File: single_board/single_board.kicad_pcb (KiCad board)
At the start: 4 copper layers, 114 parts, among them J1 CAN_OUT, J10 SPI Debug, J11 Screw_Terminal_01x02, J12 Conn_01x03, J13 Conn_01x04, J14 Screw_Terminal_01x02, J15 UART, J16 BOOTSEL, J17 Conn_01x03, J18 Conn_01x04, J19 Conn_01x03, J2 USB_C_Receptacle_USB2.0_16P, J20 Screw_Terminal_01x02, J21 Conn_01x04, J22 Conn_01x03, J23 Conn_01x04, J24 Screw_Terminal_01x02, J25 Conn_01x03, J26 Conn_01x04, J27 Screw_Terminal_01x02, J28 Screw_Terminal_01x02, J3 Conn_01x02, J5 490107670612, J6 Screw_Terminal_01x02, J7 Conn_01x03, J8 Conn_01x04, J9 SWD, Q1 AO3401A, Q2 2N7002, Q3 AO3401A, Q4 AO3401A, Q5 AO3401A, SW1 Button, U1 AP2112K-3.3, U2 TJA1042T-3, U3 USBLC6-2SC6, U4 LSM6DSV, U5 STM32G474VBTx, Y1 FC-135

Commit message: IMU
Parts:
- added D5: LED, LED_SMD:LED_0603_1608Metric_Pad1.05x0.95mm_HandSolder, F.Cu at (95.5, 169.0)
- added D6: LED, LED_SMD:LED_0603_1608Metric_Pad1.05x0.95mm_HandSolder, F.Cu at (95.5, 171.6)
- added R29: 10k, Resistor_SMD:R_0402_1005Metric_Pad0.72x0.64mm_HandSolder, F.Cu at (99.3, 168.7)
- added R30: 10k, Resistor_SMD:R_0402_1005Metric_Pad0.72x0.64mm_HandSolder, F.Cu at (99.3, 170.7)
- moved R7 91.1 mm to (98.5, 161.9)
- moved D1 91.1 mm to (95.3, 161.8)
- moved D7 42.4 mm to (96.1, 165.7), turned to 180 degrees
- moved R20 37.8 mm to (99.4, 165.7), turned to 0 degrees
- moved R21 22.3 mm to (108.6, 90.8), turned to 90 degrees
- moved J16 19.5 mm to (108.6, 94.6), turned to 90 degrees
- moved R19 16.7 mm to (113.7, 90.9), turned to -90 degrees
- moved C13 7.65 mm to (146.7, 100.3)
- moved C12 7.65 mm to (149.1, 100.3)
- moved J11 7.41 mm to (138.2, 153.4)
- moved J20 7.41 mm to (156.3, 153.5)
- moved J24 7.41 mm to (165.9, 153.5)
- moved J6 7.41 mm to (129.8, 153.4)
- moved Q2 7.41 mm to (165.7, 147.2)
- moved R16 7.41 mm to (140.9, 141.7)
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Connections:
- J20 pad 1: /FSR -> /FSR_ADC
- R23 pad 1: /FSR -> /FSR_ADC
- U5 pad 44: /FSR_SIG -> /FSR_ADC
- U5 pad 45: /FSR -> /FSR_SIG
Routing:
- net /IMU_NSS: track 4.69 -> 18.3 mm
- net /IMU_SCK: track 4.69 -> 17.8 mm
- net /IMU_MOSI: track 4.77 -> 17.3 mm, vias 0 -> 2
- net /IMU_MISO: track 4.94 -> 16.1 mm, vias 0 -> 2
- net /BOOT0: track 5.48 -> 14.2 mm
- net /TRI_LED_R: track 6.60 -> 13.5 mm
- net /FSR: track 6.92 -> 0.00 mm
- net /FSR_ADC: track 0.00 -> 6.59 mm
- net /TRI_LED_B: track 6.10 -> 12.7 mm
- net /INT1: track 4.69 -> 11.0 mm, vias 0 -> 2
- net /INT2: track 4.94 -> 11.0 mm, vias 0 -> 2
- net /TRI_LED_G: track 5.60 -> 11.6 mm
- net /PWM6: track 5.43 -> 8.83 mm
- net /DIR6: track 6.65 -> 8.58 mm
- net v3v3: vias 16 -> 17
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
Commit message: End effector gpio
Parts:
- moved D5 30.4 mm to (119.1, 149.8)
- moved D6 30.4 mm to (119.1, 152.4)
- moved R7 30.4 mm to (122.1, 142.8)
- moved D1 30.4 mm to (118.9, 142.7)
- moved R29 30.4 mm to (122.9, 149.5)
- moved R30 30.4 mm to (122.9, 151.5)
- moved D7 30.4 mm to (119.6, 146.6)
- moved R20 30.4 mm to (123.0, 146.6)
- moved J16 22.6 mm to (131.1, 93.3), turned to 180 degrees
- moved R21 18.9 mm to (127.3, 93.3), turned to 180 degrees
- moved R24 16.2 mm to (155.2, 128.5), turned to 90 degrees
- moved R14 14.4 mm to (144.1, 131.6)
- moved J24 14.0 mm to (159.5, 141.0)
- moved R19 13.9 mm to (127.4, 88.2), turned to 0 degrees
- moved Q2 13.6 mm to (159.5, 135.1)
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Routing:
- net /FSR_ADC: track 6.59 -> 10.6 mm
- net /LASER_SIG: track 6.57 -> 9.77 mm
- net /FSR_SIG: track 6.92 -> 10.1 mm
- net /LS1: track 6.44 -> 7.41 mm
- net /LS2: track 6.96 -> 7.49 mm
- net v3v3: vias 17 -> 21
- net GND: vias 29 -> 33
- added copper zone on F.Cu, net v3v3

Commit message: Layout pass 3
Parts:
- removed the R12 at (134.1, 136.3)
- removed the R14 at (144.1, 131.6)
- removed the R15 at (140.8, 136.3)
- removed the R16 at (146.3, 131.6)
- removed the R17 at (147.5, 136.3)
- removed the R2 at (141.2, 93.7)
- removed the R5 at (137.8, 93.7)
- removed the R8 at (139.6, 93.7)
- added R20: 120, Resistor_SMD:R_0402_1005Metric_Pad0.72x0.64mm_HandSolder, F.Cu at (139.1, 132.1)
- added R21: 1k, Capacitor_SMD:C_0402_1005Metric_Pad0.74x0.62mm_HandSolder, F.Cu at (140.5, 136.3)
- added R22: 120, Resistor_SMD:R_0402_1005Metric_Pad0.72x0.64mm_HandSolder, F.Cu at (143.4, 132.1)
- added R24: 1k, Capacitor_SMD:C_0402_1005Metric_Pad0.74x0.62mm_HandSolder, F.Cu at (147.0, 136.4)
- added R25: 120, Resistor_SMD:R_0402_1005Metric_Pad0.72x0.64mm_HandSolder, F.Cu at (147.8, 132.1)
- added R3: 1k, Capacitor_SMD:C_0402_1005Metric_Pad0.74x0.62mm_HandSolder, F.Cu at (138.0, 94.4)
- added R7: 1k, Capacitor_SMD:C_0402_1005Metric_Pad0.74x0.62mm_HandSolder, F.Cu at (139.3, 94.4)
- added R9: 1k, Capacitor_SMD:C_0402_1005Metric_Pad0.74x0.62mm_HandSolder, F.Cu at (136.7, 94.4)
- R18: value 120 -> 1k; footprint Resistor_SMD:R_0402_1005Metric_Pad0.72x0.64mm_HandSolder -> Capacitor_SMD:C_0402_1005Metric_Pad0.74x0.62mm_HandSolder
- moved H1 157.3 mm to (113.8, 83.5)
- moved H2 149.6 mm to (113.7, 145.8)
- moved H3 89.0 mm to (199.7, 83.6)
- moved H4 63.5 mm to (200.1, 145.1)
- moved D2 62.5 mm to (181.8, 140.2), turned to 90 degrees
- moved R2 58.9 mm to (181.8, 143.5), turned to -90 degrees
- moved D1 48.2 mm to (167.0, 140.1), turned to 90 degrees
- moved R1 44.9 mm to (166.9, 143.3), turned to -90 degrees
- moved J20 43.6 mm to (195.5, 120.0)
- moved C34 39.4 mm to (194.9, 137.8)
- moved C35 39.4 mm to (194.9, 126.5)
- moved J22 39.4 mm to (195.7, 135.1)
- moved J24 39.4 mm to (195.5, 124.0)
- moved C7 38.5 mm to (178.6, 105.5), turned to 90 degrees
- moved J23 38.0 mm to (195.8, 131.2)
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- renumbered D7 to D2, D2 to D3, D5 to D4, D6 to D5, D3 to D6, D4 to D7, J9 to J10, J10 to J11, J11 to J12, J12 to J13, J13 to J14, J14 to J15, J15 to J16, J16 to J17, J17 to J18, J18 to J19, J19 to J20, J20 to J21, J21 to J22, J22 to J23, J23 to J24, J24 to J25, J25 to J26, J26 to J27, J27 to J3, J3 to J4, J28 to J5, J5 to J6, J6 to J7, J7 to J8, J8 to J9, Q3 to Q1, Q4 to Q2, Q5 to Q3, Q1 to Q4, Q2 to Q5, R7 to R1, R9 to R10, R29 to R11, R30 to R12, R28 to R13, R10 to R14, R11 to R15, R25 to R16, R26 to R17, R13 to R19, R20 to R2, R27 to R23, R19 to R26, R21 to R27, R22 to R28, R23 to R29, R24 to R30, R1 to R4, R3 to R5, R4 to R6, R6 to R8
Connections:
- D3 pad 3: 5V -> v3v3
- D4 pad 2: unconnected-(D5-A-Pad2) -> /LED1
- D5 pad 2: unconnected-(D6-A-Pad2) -> /LED2
- R18 pad 1: /LimitSwitch3 -> v3v3
- R18 pad 2: /LS3 -> /LimitSwitch1
- U5 pad 30: /HEARTBEAT -> /LED1
- U5 pad 31: unconnected-(U5-PC5-Pad31) -> /LED2
- U5 pad 58: unconnected-(U5-PD11-Pad58) -> /HEARTBEAT
- U5 pad 92: /TRI_LED_R -> /TRI_LED_G
- U5 pad 93: /TRI_LED_B -> /TRI_LED_R
- U5 pad 94: /TRI_LED_G -> /TRI_LED_B
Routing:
- net /CAN_STB: track 6.27 -> 17.3 mm
- net /FDCAN_TX: track 6.34 -> 11.3 mm
- net /LED1: track 0.00 -> 4.71 mm
- net /HEARTBEAT: track 4.71 -> 0.00 mm
- net /FDCAN_RX: track 5.94 -> 9.92 mm
- net /TRI_LED_G: track 11.6 -> 13.5 mm
- net /TRI_LED_B: track 12.7 -> 11.6 mm
- net /TRI_LED_R: track 13.5 -> 12.7 mm
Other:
- board outline added: 94.5 x 70.3 mm

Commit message: Pos
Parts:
- moved R19 34.7 mm to (142.7, 88.2), turned to 180 degrees
- moved C28 33.1 mm to (142.7, 86.2), turned to 180 degrees
- moved SW1 28.2 mm to (147.8, 87.2), turned to 180 degrees
- moved D2 27.5 mm to (158.9, 124.9)
- moved R2 27.5 mm to (158.9, 128.2)
- moved D1 16.0 mm to (161.8, 125.0)
- moved R1 16.0 mm to (161.7, 128.2)
- moved Q3 11.4 mm to (168.7, 86.5), turned to 180 degrees
- moved H4 10.2 mm to (189.9, 144.8)
- moved J6 9.89 mm to (160.3, 87.4), turned to -90 degrees
- moved D6 9.65 mm to (173.8, 92.0)
- moved D7 9.65 mm to (173.8, 99.1)
- moved J3 9.65 mm to (188.2, 90.1)
- moved J4 9.65 mm to (182.0, 90.0)
- moved J5 9.65 mm to (188.2, 97.0)
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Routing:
- net /LED2: track 0.00 -> 5.63 mm
- net /LED1: track 4.71 -> 4.11 mm
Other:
- board size 94.5 x 70.3 mm -> 85.3 x 71.2 mm

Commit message: Signal Traces
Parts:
- moved D4 5.95 mm to (120.8, 140.6)
- moved R11 5.95 mm to (120.7, 143.6)
- moved D5 3.43 mm to (125.8, 140.6)
- moved R12 3.43 mm to (125.8, 143.7)
- moved C2 0.84 mm to (166.7, 128.3)
- moved C8 0.84 mm to (170.8, 139.2)
- moved C9 0.84 mm to (165.5, 131.5)
- moved R10 0.84 mm to (170.2, 137.4)
- moved R5 0.84 mm to (171.0, 136.4)
- moved R8 0.84 mm to (170.5, 134.6)
- moved U2 0.84 mm to (170.5, 129.8)
- moved C1 0.83 mm to (165.6, 128.3)
- moved C10 0.83 mm to (166.6, 131.5)
- moved R24 0.83 mm to (147.8, 136.3)
- moved R25 0.75 mm to (148.5, 132.1), turned to 90 degrees
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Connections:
- U5 pad 50: /CAN_LED -> unconnected-(U5-PB11-Pad50)
- U5 pad 54: unconnected-(U5-PB15-Pad54) -> /CAN_LED
- U5 pad 55: unconnected-(U5-PD8-Pad55) -> /HEARTBEAT
- U5 pad 58: /HEARTBEAT -> unconnected-(U5-PD11-Pad58)
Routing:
- net /RST: track 1.67 -> 74.2 mm, vias 1 -> 2
- net /PWM5: track 8.19 -> 39.4 mm
- net /PWM4: track 6.98 -> 37.0 mm
- net /ENC4_B: track 9.40 -> 37.9 mm
- net /ENC5_B: track 7.02 -> 34.7 mm
- net /LED1: track 4.11 -> 31.7 mm, vias 0 -> 2
- net /DIR5: track 8.92 -> 36.4 mm
- net /ENC4_A: track 9.01 -> 35.7 mm
- net /DIR4: track 7.06 -> 33.3 mm
- net 5V: track 0.00 -> 26.2 mm, vias 0 -> 2
- net /ENC5_A: track 7.08 -> 32.1 mm
- net /ENC3_B: track 4.57 -> 29.5 mm
- net /LED2: track 5.63 -> 27.7 mm, vias 0 -> 2
- net /PWM6: track 8.83 -> 30.4 mm
- net /SWDIO: track 6.43 -> 26.7 mm
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- added copper zone on B.Cu, net GND
- added copper zone on F.Cu, net GND
- added copper zone on In2.Cu, net GND
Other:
- board size 85.3 x 71.2 mm -> 90 x 70 mm

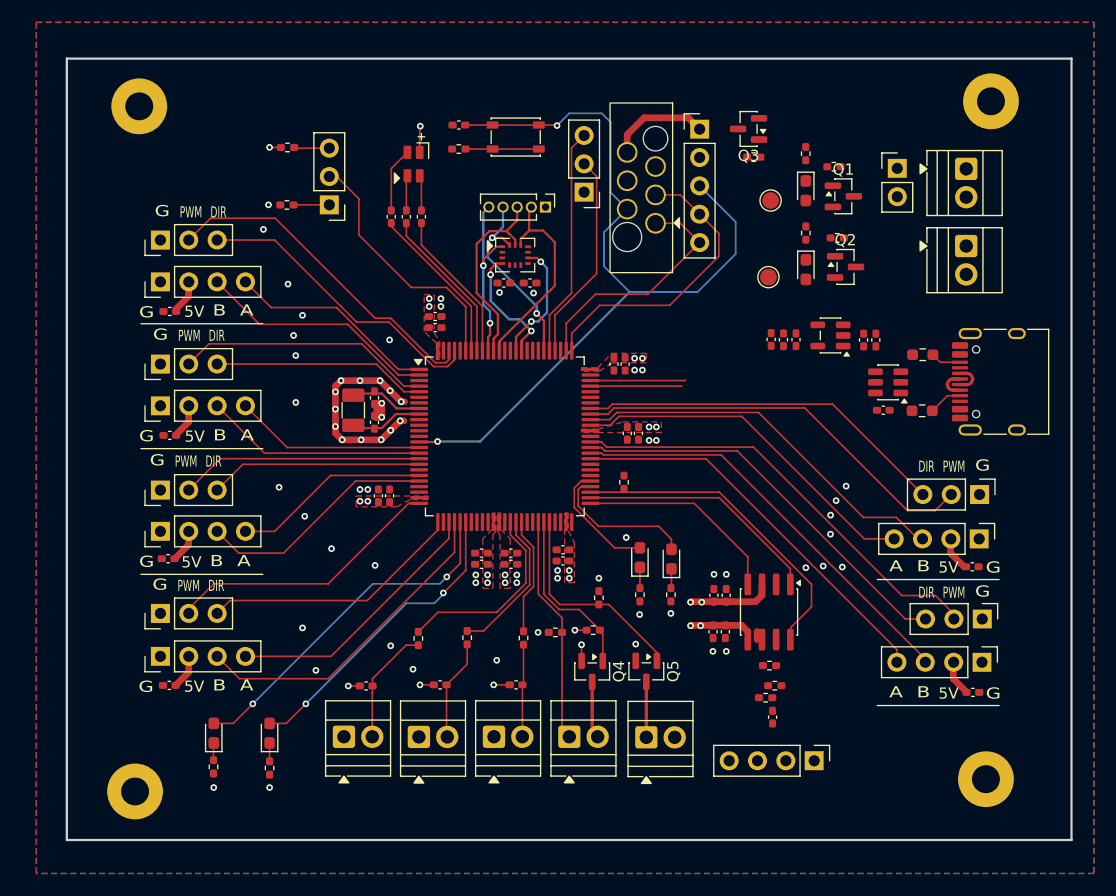
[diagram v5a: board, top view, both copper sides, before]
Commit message: Diff pairs, layer 1 power
Net classes and rules
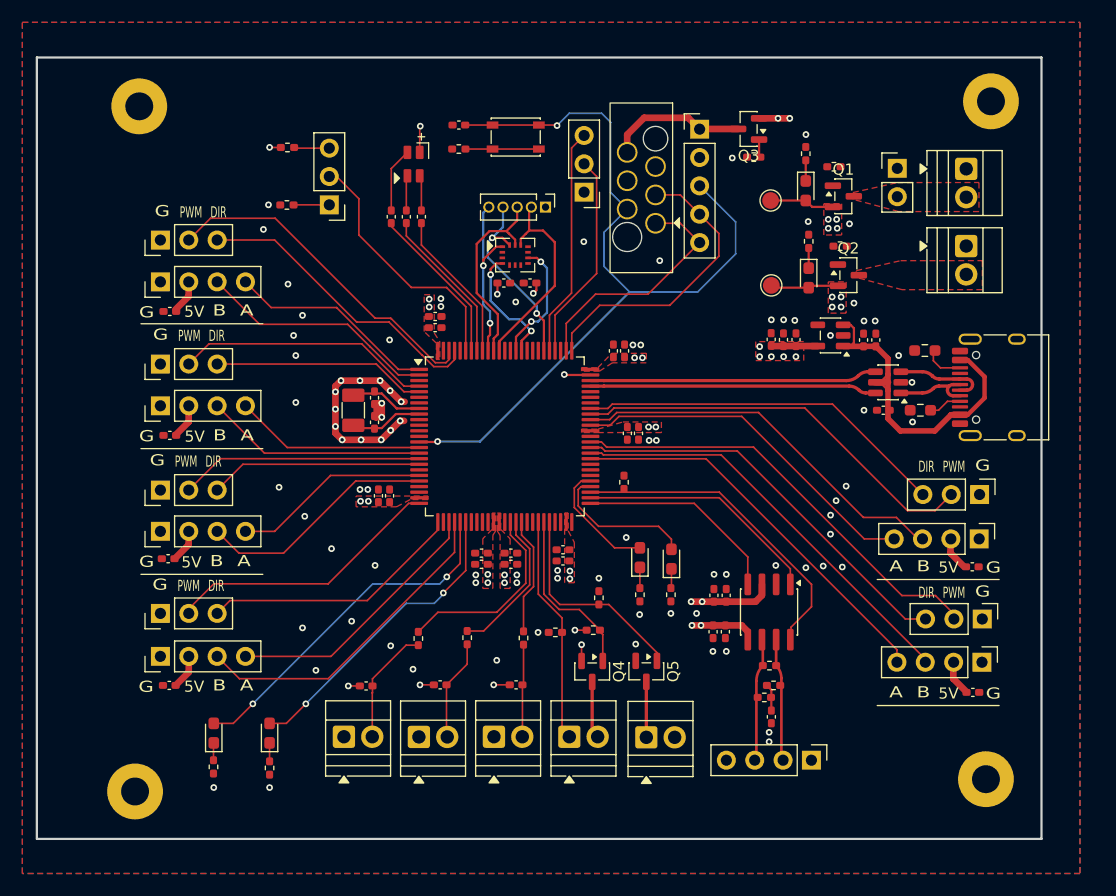
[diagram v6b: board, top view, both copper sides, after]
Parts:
- moved C15 1.19 mm to (157.6, 106.4), turned to 90 degrees
- moved C21 1.19 mm to (156.6, 106.4), turned to 90 degrees
- moved R17 0.78 mm to (176.9, 97.0)
- moved D7 0.78 mm to (174.0, 99.8)
- moved Q2 0.78 mm to (177.6, 99.6)
- moved R15 0.78 mm to (174.0, 96.6)
- moved TP2 0.78 mm to (170.7, 100.5)
- moved J2 0.50 mm to (191.6, 109.7)
- moved R6 0.42 mm to (184.4, 106.3)
- moved J1 0.25 mm to (174.3, 143.1)
- moved R4 0.17 mm to (184.1, 111.7)
- moved C8 0.11 mm to (170.7, 139.2)
- moved R10 0.11 mm to (170.1, 137.4)
- moved R5 0.11 mm to (170.9, 136.3)
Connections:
- net Net-(J2-D+-PadA6) renamed /DP
- net Net-(J2-D--PadA7) renamed /DN
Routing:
- net 5V: track 26.2 -> 63.8 mm, vias 2 -> 6
- net /USB-DN: track 8.21 -> 25.7 mm
- net /USB-DP: track 8.52 -> 25.7 mm
- net v3v3: track 15.0 -> 29.9 mm, vias 9 -> 37
- net /can_DP: track 0.00 -> 11.0 mm
- net /can_DN: track 0.72 -> 11.0 mm
- net /DP: track 2.93 -> 8.40 mm
- net /DN: track 2.93 -> 7.42 mm
- net /v3v3IN: track 9.13 -> 12.6 mm
- net Net-(C8-Pad1): track 0.00 -> 2.42 mm
- net GND: track 22.3 -> 24.7 mm, vias 81 -> 88
- net Net-(D6-K): track 0.00 -> 1.85 mm
- net Net-(D7-K): track 0.00 -> 1.80 mm
- net Net-(Q3-G): track 0.00 -> 1.62 mm
- net Net-(J2-CC2): track 2.70 -> 3.63 mm
- added copper zone on F.Cu, net /5VIN
- added copper zone on F.Cu, net 5V
- added copper zone on In1.Cu, net 5V
- added copper zone on In1.Cu, net v3v3

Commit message: 80x80
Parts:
- moved J4 59.6 mm to (217.5, 137.9)
- moved TP1 59.6 mm to (206.2, 140.8)
- moved D6 59.6 mm to (209.3, 139.9)
- moved J3 59.6 mm to (223.7, 138.0)
- moved Q1 59.6 mm to (212.7, 140.4)
- moved R14 59.6 mm to (209.3, 136.6)
- moved R16 59.6 mm to (211.8, 137.8)
- moved H2 9.48 mm to (120.4, 152.6)
- moved H4 7.81 mm to (190.4, 152.6)
- moved H1 6.61 mm to (120.4, 82.5)
- moved C4 5.51 mm to (173.4, 105.3)
- moved C3 5.51 mm to (174.6, 105.3)
- moved C5 5.51 mm to (167.4, 105.2)
- moved C6 5.51 mm to (166.3, 105.2)
- moved C7 5.51 mm to (165.2, 105.2)
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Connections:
- J10 pad 1: /v3v3IN -> /v3v3IN_debug
- J6 pad 6: /v3v3IN -> /v3v3IN_debug
- Q3 pad 3: /v3v3IN -> /v3v3IN_debug
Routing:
- net v3v3: track 29.9 -> 274.7 mm, vias 37 -> 36
- net 5V: track 63.8 -> 141.6 mm, vias 6 -> 10
- net /v3v3IN_debug: track 0.00 -> 12.6 mm
- net /v3v3IN: track 12.6 -> 0.00 mm
- net Net-(Q1-G): track 0.00 -> 1.91 mm
- net Net-(Q2-G): track 0.00 -> 1.82 mm
- net GND: vias 88 -> 98
- added copper zone on F.Cu, net /v3v3IN
- added copper zone on In2.Cu, net 5V
- added copper zone on In2.Cu, net v3v3
- removed copper zone on In1.Cu, net 5V
- removed copper zone on In1.Cu, net v3v3
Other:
- board size 90 x 70 mm -> 80 x 80 mm

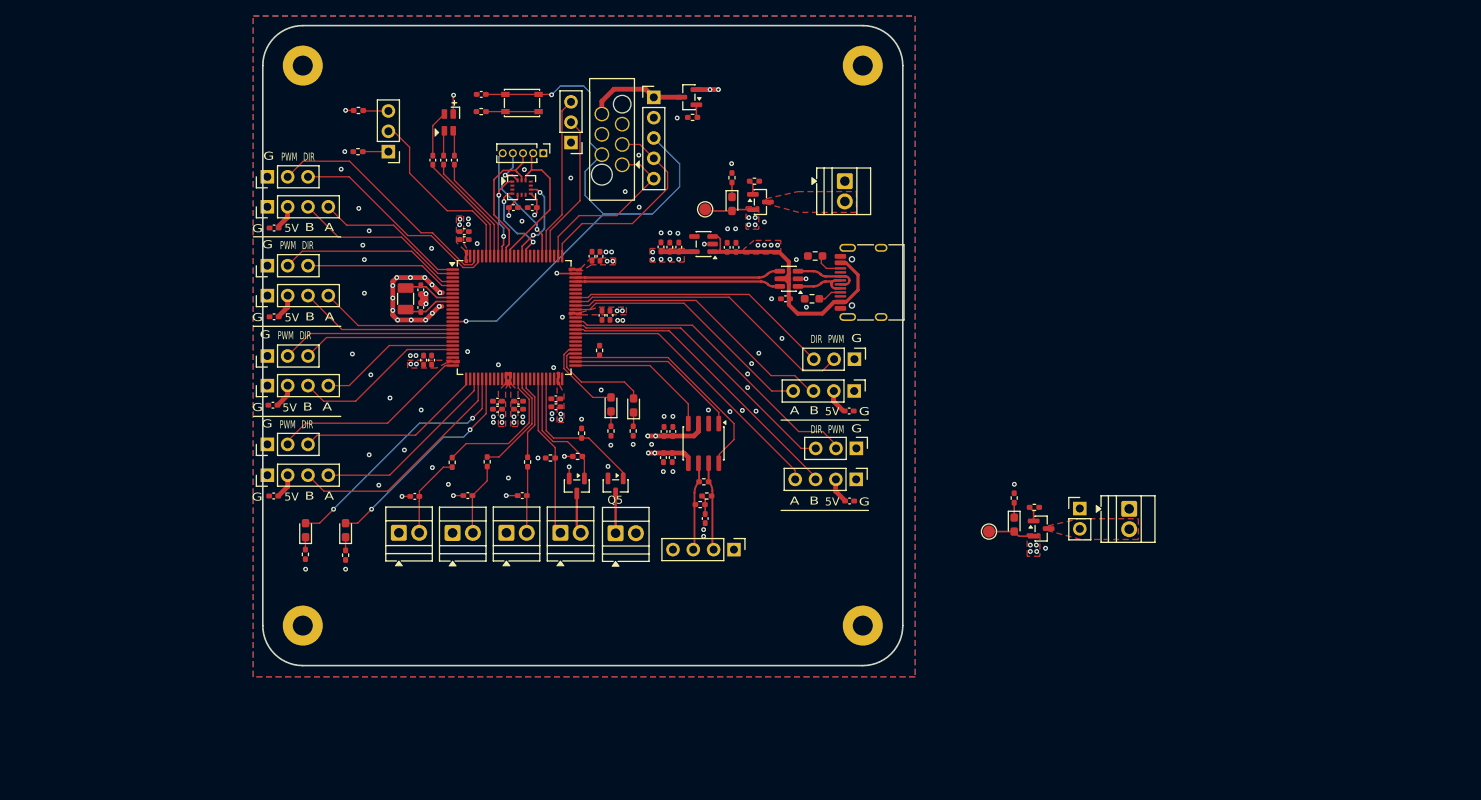
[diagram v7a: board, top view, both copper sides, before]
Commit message: All sig
todo: power, silkscreen, vias
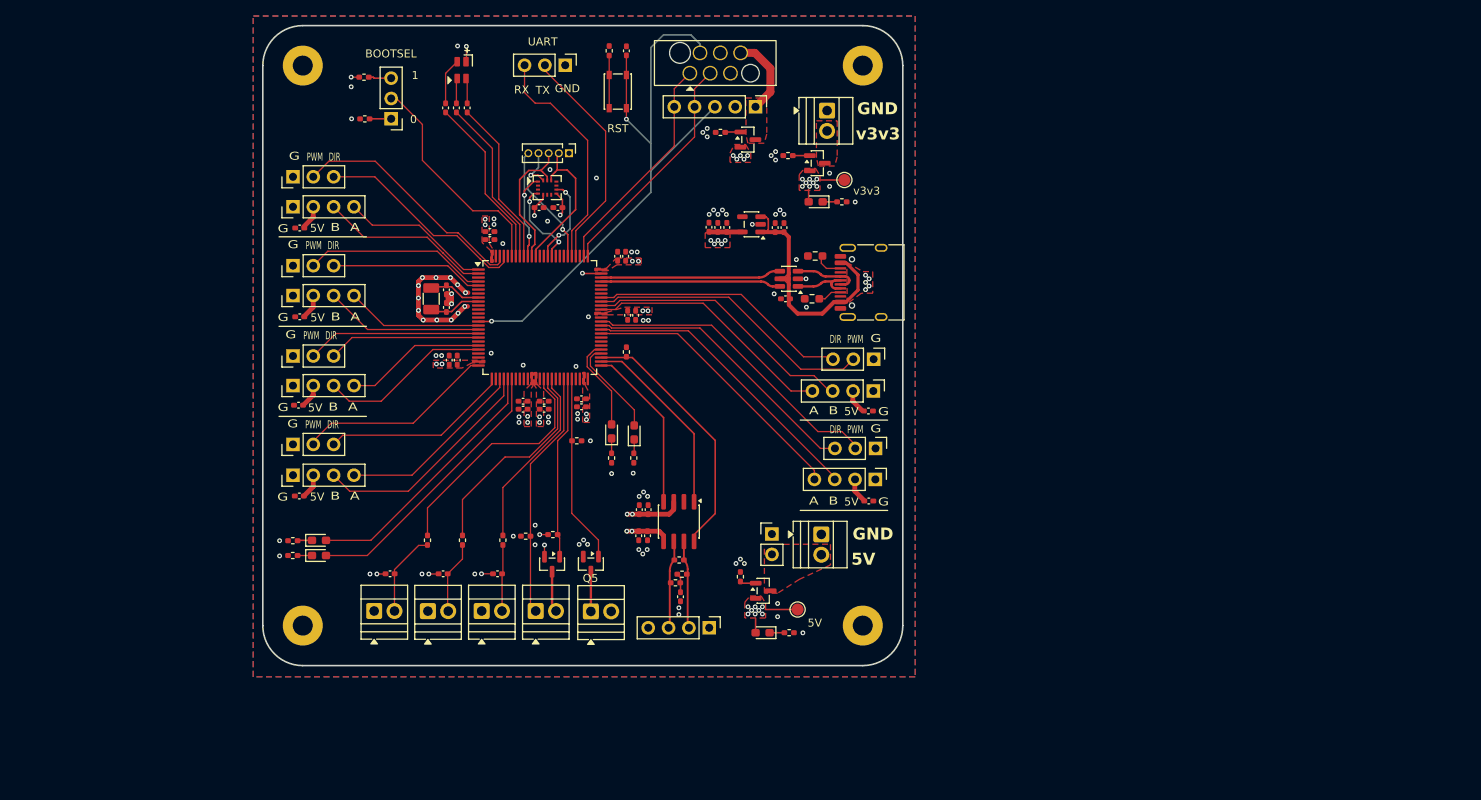
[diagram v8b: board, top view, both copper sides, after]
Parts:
- moved J4 38.6 mm to (179.0, 141.1)
- moved J3 38.6 mm to (185.2, 141.2)
- moved R16 37.8 mm to (175.1, 146.4), turned to 90 degrees
- moved Q1 35.6 mm to (177.9, 148.2)
- moved D6 34.2 mm to (177.9, 153.4), turned to 180 degrees
- moved R14 32.8 mm to (181.2, 153.4), turned to 0 degrees
- moved TP1 25.8 mm to (182.2, 150.5)
- moved C28 18.9 mm to (160.8, 80.7), turned to 90 degrees
- moved TP2 17.8 mm to (188.1, 96.8), turned to -90 degrees
- moved R19 17.7 mm to (158.7, 80.7), turned to 90 degrees
- moved J6 16.5 mm to (176.4, 83.5), turned to 180 degrees
- moved R15 14.1 mm to (187.8, 99.6), turned to 0 degrees
- moved J10 12.8 mm to (177.0, 87.7), turned to -90 degrees
- moved SW1 12.1 mm to (159.8, 85.8), turned to 90 degrees
- moved D7 10.5 mm to (184.5, 99.6), turned to 180 degrees
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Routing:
- net v3v3: track 274.7 -> 29.2 mm, vias 36 -> 43
- net 5V: track 141.6 -> 83.0 mm, vias 10 -> 15
- net GND: track 24.7 -> 55.3 mm, vias 98 -> 91
- net /LS2: track 13.5 -> 26.8 mm
- net /LS1: track 17.5 -> 30.2 mm
- net /LS3: track 10.6 -> 23.0 mm
- net /CAN_STB: track 29.0 -> 39.6 mm
- net /FSR_ADC: track 20.4 -> 31.0 mm
- net /UART4_TX: track 18.7 -> 28.6 mm
- net /UART4_RX: track 20.6 -> 29.1 mm
- net /ENC4_B: track 37.9 -> 46.3 mm
- net /TRI_LED_B: track 14.4 -> 21.6 mm
- net /TRI_LED_G: track 13.7 -> 20.9 mm
- net /TRI_LED_R: track 14.0 -> 21.2 mm
- net /FSR_SIG: track 15.7 -> 22.9 mm
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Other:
- board text added: "0"
- board text added: "1"
- board text added: "BOOTSEL"
- board text added: "GND"
- board text added: "RST"
- board text added: "RX"
- board text added: "TX"
- board text added: "UART"
- board text added: "v3v3"
